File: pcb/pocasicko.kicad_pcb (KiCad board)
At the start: 2 copper layers, 100 x 100 mm, 15 parts, among them J1 SMA, J2 Header_SMD_01x06, J3 FPC24, Q1 Si2312, SW1 SW_Push, SW2 SW_Push, SW3 SW_Push, SW4 SW_Push, SW5 SW_Push, U1 CMWX1ZZABZ-091, U2 BME680

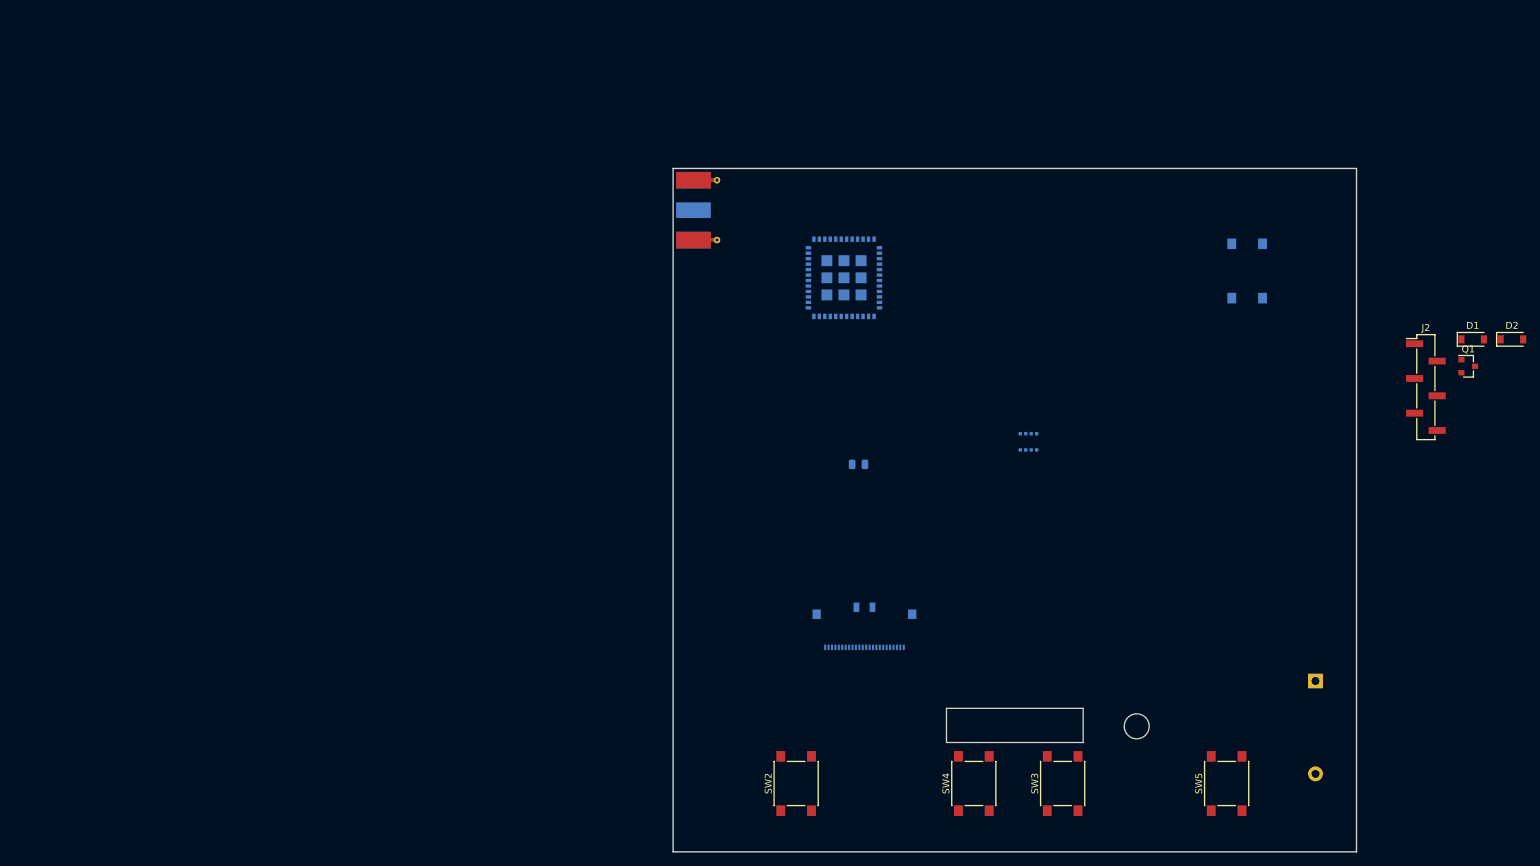
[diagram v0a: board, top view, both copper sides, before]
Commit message: Finish schematic and large component placement
All components chosen and placed on the PCB before routing and
schematic probably mostly finished.
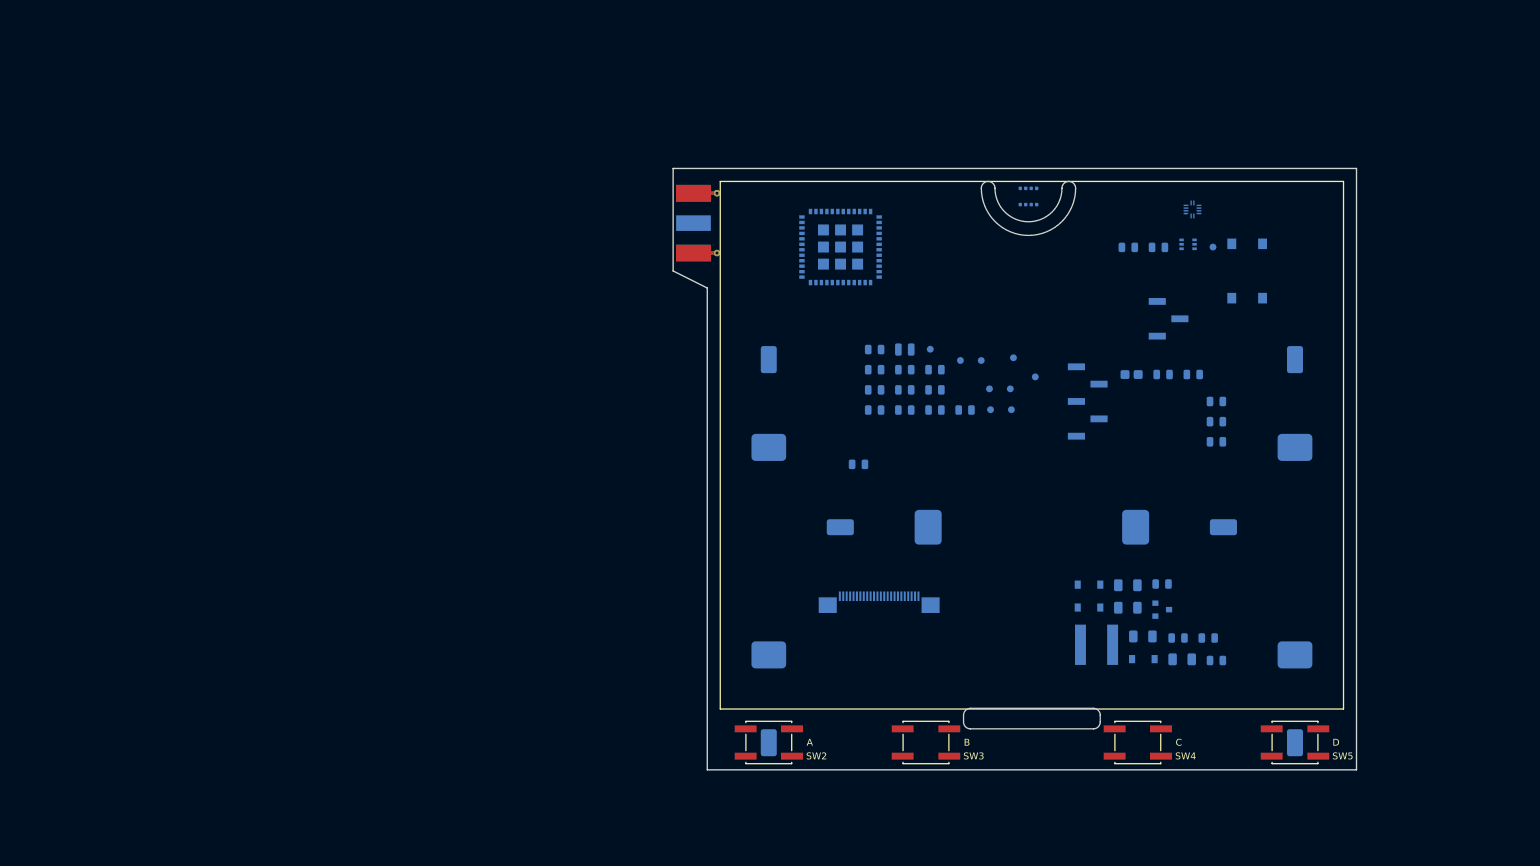
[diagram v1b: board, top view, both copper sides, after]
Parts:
- added BT2: AA, Moje:BatteryHolder_Keystone_53_1xAA, B.Cu at (152.5, 102.5)
- added BT3: AA, Moje:BatteryHolder_Keystone_53_1xAA, B.Cu at (114.0, 106.0)
- added C10: 1uF/6V, Capacitor_SMD:C_0805_2012Metric, B.Cu at (138.3, 85.3)
- added C11: 100nF, Capacitor_SMD:C_0805_2012Metric, B.Cu at (129.5, 76.5)
- added C12: 1uF/25V, Capacitor_SMD:C_0805_2012Metric, B.Cu at (133.9, 79.5)
- added C13: 1uF/25V, Capacitor_SMD:C_0805_2012Metric, B.Cu at (138.3, 82.4)
- added C14: 1uF/25V, Capacitor_SMD:C_0805_2012Metric, B.Cu at (142.7, 85.3)
- added C15: 1uF/50V, Capacitor_SMD:C_1206_3216Metric, B.Cu at (166.5, 114.3)
- added C16: 4.7uF/50V, Capacitor_SMD:C_1206_3216Metric, B.Cu at (168.7, 118.5)
- added C17: 10uF/6V, Capacitor_SMD:C_0805_2012Metric, B.Cu at (173.9, 118.7)
- added C18: 1uF/50V, Capacitor_SMD:C_1206_3216Metric, B.Cu at (174.5, 121.8)
- added C19: 100nF, Capacitor_SMD:C_0805_2012Metric, B.Cu at (179.5, 122.0)
- added C2: 10uF, Capacitor_SMD:C_0805_2012Metric, B.Cu at (129.5, 85.3)
- added C3: 10uF, Capacitor_SMD:C_0805_2012Metric, B.Cu at (179.5, 90.0)
- added C4: 1uF, Capacitor_SMD:C_0805_2012Metric, B.Cu at (171.7, 80.2)
- added C5: 100nF, Capacitor_SMD:C_0805_2012Metric, B.Cu at (179.5, 87.0)
- added C6: 10uF, Capacitor_SMD:C_0805_2012Metric, B.Cu at (129.5, 82.4)
- added C7: 1uF/25V, Capacitor_SMD:C_0805_2012Metric, B.Cu at (133.9, 85.3)
- added C8: 1uF/25V, Capacitor_SMD:C_0805_2012Metric, B.Cu at (129.5, 79.5)
- added C9: 1uF/25V, Capacitor_SMD:C_0805_2012Metric, B.Cu at (133.9, 82.4)
- added D3: LED, LED_SMD:LED_0805_2012Metric_Castellated, B.Cu at (167.1, 80.2)
- added D4: MBR0530, Diode_SMD:D_SOD-123, B.Cu at (160.9, 110.9)
- added G***: LOGO, Moje:moje_logo, B.Cu at (152.0, 70.5)
- added J4: Header_SMD_1x03, Connector_PinHeader_2.54mm:PinHeader_1x03_P2.54mm_Vertical_SMD_Pin1Left, B.Cu at (172.5, 72.0)
- added L1: DFE201612P-2R2M, Moje:L_0806_2016Metric, B.Cu at (133.9, 76.5)
- added L2: NRS6045T680MMGK, Inductor_SMD:L_Taiyo-Yuden_NR-60xx, B.Cu at (162.0, 119.7)
- added R1: 100k, Resistor_SMD:R_0805_2012Metric, B.Cu at (176.1, 80.2)
- added R2: 1k, Resistor_SMD:R_0805_2012Metric, B.Cu at (179.5, 84.1)
- added R3: 100k, Resistor_SMD:R_0805_2012Metric, B.Cu at (138.3, 79.5)
- added R4: 10k, Resistor_SMD:R_0805_2012Metric, B.Cu at (178.3, 118.7)
- added R5: 0R47, Resistor_SMD:R_1206_3216Metric, B.Cu at (166.5, 111.0)
- added R6: 0R, Resistor_SMD:R_0805_2012Metric, B.Cu at (171.6, 110.8)
- added R7: 0R, Resistor_SMD:R_0805_2012Metric, B.Cu at (166.6, 61.5)
- added R8: 0R, Resistor_SMD:R_0805_2012Metric, B.Cu at (171.0, 61.5)
- added TP1: CRF1, TestPoint:TestPoint_Pad_D1.0mm, B.Cu at (146.4, 85.3)
- added TP10: PB14, TestPoint:TestPoint_Pad_D1.0mm, B.Cu at (179.0, 61.5)
- added TP2: CRF2, TestPoint:TestPoint_Pad_D1.0mm, B.Cu at (137.6, 76.5)
- added TP3: CRF3, TestPoint:TestPoint_Pad_D1.0mm, B.Cu at (142.0, 78.1)
- added TP4: DIO0, TestPoint:TestPoint_Pad_D1.0mm, B.Cu at (146.3, 82.2)
- added TP5: DIO1, TestPoint:TestPoint_Pad_D1.0mm, B.Cu at (149.5, 85.3)
- added TP6: DIO2, TestPoint:TestPoint_Pad_D1.0mm, B.Cu at (149.8, 77.7)
- added TP7: DIO3, TestPoint:TestPoint_Pad_D1.0mm, B.Cu at (145.1, 78.1)
- added TP8: DIO4, TestPoint:TestPoint_Pad_D1.0mm, B.Cu at (149.3, 82.2)
- added TP9: DIO5, TestPoint:TestPoint_Pad_D1.0mm, B.Cu at (153.0, 80.5)
- added U3: MP28200, Moje:QFN-12_2x2_Pitch0.4mm, B.Cu at (176.0, 56.0)
- added U4: LM66100, Package_TO_SOT_SMD:SOT-363_SC-70-6, B.Cu at (175.3, 61.1)
- BT1: value 2xAA -> AA; footprint Battery:BatteryHolder_MPD_BC2AAPC_2xAA -> Moje:BatteryHolder_Keystone_53_1xAA
- D1, D2: value D_Schottky -> MBR0530; moved to B.Cu
- J2: value Header_SMD_01x06 -> Header_SMD_1x05; footprint Connector_PinHeader_2.54mm:PinHeader_1x06_P2.54mm_Vertical_SMD_Pin1Left -> Connector_PinHeader_2.54mm:PinHeader_1x05_P2.54mm_Vertical_SMD_Pin1Left; moved to B.Cu
- J3: footprint Connector_FFC-FPC:Molex_502244-2430_1x24-1MP_P0.5mm_Horizontal -> Moje:Waveshare_EPD_4.2_Amphenol_SFV24R-4STBE1HLF
- Q1: value Si2312 -> AO3400A; moved to B.Cu
- SW2: value SW_Push -> A; footprint Button_Switch_SMD:SW_Push_1P1T_NO_6x6mm_H9.5mm -> Button_Switch_SMD:SW_SPST_EVQQ2
- SW3: value SW_Push -> B; footprint Button_Switch_SMD:SW_Push_1P1T_NO_6x6mm_H9.5mm -> Button_Switch_SMD:SW_SPST_EVQQ2
- SW4: value SW_Push -> C; footprint Button_Switch_SMD:SW_Push_1P1T_NO_6x6mm_H9.5mm -> Button_Switch_SMD:SW_SPST_EVQQ2
- SW5: value SW_Push -> D; footprint Button_Switch_SMD:SW_Push_1P1T_NO_6x6mm_H9.5mm -> Button_Switch_SMD:SW_SPST_EVQQ2
- moved D2 71.4 mm to (168.8, 121.8)
- moved D1 68.5 mm to (160.9, 114.2)
- moved Q1 57.2 mm to (171.6, 114.6)
- moved J2 49.5 mm to (160.7, 84.1)
- moved J3 36.8 mm to (152.5, 89.5), turned to 180 degrees
- moved U2 35.9 mm to (152.0, 54.1)
- moved SW4 24.7 mm to (168.0, 134.0), turned to 0 degrees
- moved SW3 20.9 mm to (137.0, 134.0), turned to 0 degrees
- moved BT1 19.2 mm to (191.0, 106.0), turned to -90 degrees
- moved SW5 11.7 mm to (191.0, 134.0), turned to 0 degrees
- moved SW2 7.21 mm to (114.0, 134.0), turned to 0 degrees
- moved U1 4.53 mm to (124.5, 61.5), turned to 180 degrees
- moved J1 1.90 mm to (104.7, 58.0)
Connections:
- net Net-(J3-Pad19) renamed /VPP
- net Net-(J3-Pad6) renamed /TSCL
- net Net-(J3-Pad7) renamed /TSDA
- net Net-(U1-Pad35) renamed /BME680_SCL
- net Net-(U1-Pad36) renamed /BME680_SDA
- BT1 pad 1: +BATT -> Net-(BT1-Pad1)
- BT1 pad 2: Net-(BT1-Pad2) -> GND
- C1 pad 1: /Reset -> /~MCU_RESET
- C1 pad 2: Net-(C1-Pad2) -> GND
- D1 pad 1: Net-(C2-Pad1) -> GND
- D1 pad 2: Net-(D1-Pad2) -> Net-(C16-Pad2)
- D2 pad 1: Net-(D2-Pad1) -> Net-(C16-Pad2)
- D2 pad 2: Net-(C2-Pad1) -> /PREVGL
- J2 pad 1: Net-(J2-Pad1) -> +2V5
- J2 pad 5: /NRST -> /~MCU_RESET
- J3 pad 10: Net-(J3-Pad10) -> /RES#
- J3 pad 11: Net-(J3-Pad11) -> /D/C#
- J3 pad 12: Net-(J3-Pad12) -> /CS#
- J3 pad 13: Net-(J3-Pad13) -> /SCLK
- J3 pad 14: Net-(J3-Pad14) -> /SDI
- J3 pad 15: Net-(J3-Pad15) -> +2V5
- J3 pad 16: Net-(J3-Pad16) -> +2V5
- J3 pad 17: Net-(J3-Pad17) -> GND
- J3 pad 18: Net-(J3-Pad18) -> /VDD
- J3 pad 2: Net-(J3-Pad2) -> /GDR
- J3 pad 20: Net-(J3-Pad20) -> /VSH
- J3 pad 21: Net-(J3-Pad21) -> /PREVGH
- J3 pad 22: Net-(J3-Pad22) -> /VSL
- J3 pad 23: Net-(J3-Pad23) -> /PREVGL
- J3 pad 24: Net-(J3-Pad24) -> /VCOM
- J3 pad 3: Net-(J3-Pad3) -> /RESE
- J3 pad 4: Net-(J3-Pad4) -> /VGL
- J3 pad 5: Net-(J3-Pad5) -> /VGH
- J3 pad 8: Net-(J3-Pad8) -> /BS1
- J3 pad 9: Net-(J3-Pad9) -> /BUSY
- Q1 pad 1: +BATT -> /GDR
- Q1 pad 2: GND -> /RESE
- Q1 pad 3: Net-(BT1-Pad2) -> Net-(C16-Pad1)
- SW1 pad 2: Net-(C1-Pad2) -> /~MCU_RESET
- SW2 pad 1: Net-(SW2-Pad1) -> /BUTTON_A
- SW2 pad 2: Net-(SW2-Pad2) -> GND
- SW3 pad 1: Net-(SW3-Pad1) -> /BUTTON_B
- SW3 pad 2: Net-(SW3-Pad2) -> GND
- SW4 pad 1: Net-(SW4-Pad1) -> /BUTTON_C
- SW4 pad 2: Net-(SW4-Pad2) -> GND
- SW5 pad 1: Net-(SW5-Pad1) -> /BUTTON_D
- SW5 pad 2: Net-(SW5-Pad2) -> GND
- U1 pad 14: Net-(U1-Pad14) -> /SDI
- U1 pad 16: Net-(U1-Pad16) -> /SCLK
- U1 pad 17: Net-(U1-Pad17) -> /CS#
- U1 pad 18: Net-(U1-Pad18) -> /USART1_RX
- U1 pad 19: Net-(U1-Pad19) -> /USART1_TX
- U1 pad 2: Net-(U1-Pad2) -> /LED
- U1 pad 21: Net-(U1-Pad21) -> /BUTTON_D
- U1 pad 22: Net-(U1-Pad22) -> /BUTTON_C
- U1 pad 23: Net-(U1-Pad23) -> /BUTTON_B
- U1 pad 24: Net-(U1-Pad24) -> /BATT_VOLTAGE
- U1 pad 32: Net-(U1-Pad32) -> +2V5
- U1 pad 33: Net-(U1-Pad33) -> /BUTTON_A
- U1 pad 34: /Reset -> /~MCU_RESET
- U1 pad 37: Net-(U1-Pad37) -> /D/C#
- U1 pad 39: Net-(U1-Pad39) -> /RES#
- U1 pad 4: Net-(U1-Pad4) -> +2V5
- U1 pad 40: Net-(U1-Pad40) -> /BUSY
- U1 pad 41: /SWCLK -> /SWDIO
- U1 pad 42: /SWDIO -> /SWCLK
- U1 pad 46: Net-(U1-Pad46) -> /TCXO_OUT
- U1 pad 47: Net-(U1-Pad47) -> /TCXO_OUT
- U1 pad 48: Net-(U1-Pad48) -> Net-(U1-Pad1)
- U1 pad 5: Net-(U1-Pad5) -> +2V5
- U1 pad 6: Net-(U1-Pad6) -> +2V5
- U2 pad 6: +3V3 -> +2V5
- U2 pad 8: +3V3 -> +2V5
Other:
- board size 100 x 100 mm -> 100 x 88 mm
- board text added: "Počasíčko 10/2019 Rev.1 Radovan Blažek"

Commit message: Routing progress
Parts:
- added C20: 1uF, Capacitor_SMD:C_0805_2012Metric, B.Cu at (116.0, 59.1)
- added H1: M3_Hole, MountingHole:MountingHole_3.2mm_M3_DIN965_Pad, F.Cu at (126.0, 134.0)
- added H2: M3_Hole, MountingHole:MountingHole_3.2mm_M3_DIN965_Pad, F.Cu at (180.0, 134.0)
- added REF**: KiCad-Logo_5mm_SilkScreen, Symbol:KiCad-Logo_5mm_SilkScreen, B.Cu at (187.9, 58.6)
- moved R7 56.9 mm to (110.6, 71.5)
- moved R1 56.1 mm to (126.8, 53.5)
- moved C3 55.5 mm to (133.9, 58.4), turned to 180 degrees
- moved C19 54.2 mm to (127.0, 108.5), turned to -90 degrees
- moved R2 53.3 mm to (133.9, 56.5)
- moved C5 52.9 mm to (133.9, 60.3), turned to 180 degrees
- moved TP10 52.3 mm to (127.3, 69.6)
- moved TP6 51.1 mm to (138.7, 27.9)
- moved TP8 51.1 mm to (138.2, 32.4)
- moved TP9 51.1 mm to (141.9, 30.6)
- moved TP4 51.1 mm to (135.2, 32.4)
- moved TP5 51.1 mm to (138.4, 35.5)
- moved TP7 51.1 mm to (134.0, 28.2)
- moved R6 50.6 mm to (121.0, 108.5), turned to 90 degrees
- moved U3 48.6 mm to (141.7, 90.4), turned to 180 degrees
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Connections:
- C12 pad 2: +2V5 -> /VPP
- U2 pad 2: +3V3 -> +2V5
- U3 pad 1: Net-(L1-Pad1) -> +2V5
- U3 pad 9: +2V5 -> Net-(L1-Pad1)
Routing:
- net /D/C#: track 0.00 -> 106.9 mm, vias 0 -> 2
- net /RES#: track 0.00 -> 101.8 mm, vias 0 -> 2
- net /BUSY: track 0.00 -> 97.2 mm, vias 0 -> 2
- net /SDI: track 0.00 -> 76.4 mm, vias 0 -> 2
- net /SCLK: track 0.00 -> 73.0 mm, vias 0 -> 2
- net /CS#: track 0.00 -> 70.1 mm, vias 0 -> 2
- net +2V5: track 0.00 -> 60.5 mm, vias 0 -> 2
- net /~MCU_RESET: track 0.00 -> 59.0 mm, vias 0 -> 2
- net Net-(BT2-Pad1): track 0.00 -> 53.1 mm
- net GND: track 0.00 -> 51.7 mm, vias 0 -> 42
- net /BME680_SCL: track 0.00 -> 47.6 mm
- net Net-(BT1-Pad1): track 0.00 -> 45.4 mm
- net /BME680_SDA: track 0.00 -> 43.6 mm
- net /GDR: track 0.00 -> 36.7 mm
- net /RESE: track 0.00 -> 30.6 mm
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- added copper zone on B.Cu, net +2V5
- added copper zone on B.Cu, net /BATT_VOLTAGE
- added copper zone on B.Cu, net GND
- added copper zone on F.Cu, net GND
- added copper zone on B.Cu, net Net-(J1-Pad1)
- added copper zone on B.Cu, net Net-(L1-Pad1)
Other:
- net class Default: clearance 0.2 -> 0.127
- rule pad_to_mask_clearance: 0.051 -> 0
- rule solder_mask_min_width: 0.25 -> 0.12
- rule trace_clearance: 0.2 -> 0.127
- rule trace_min: 0.2 -> 0.127
- rule via_min_size: 0.4 -> 0.6
- board text added: "GND"
- board text added: "NRST"
- board text added: "RX"
- board text added: "SWCLK"
- board text added: "SWDIO"
- board text added: "TX"
- board text added: "VDD"

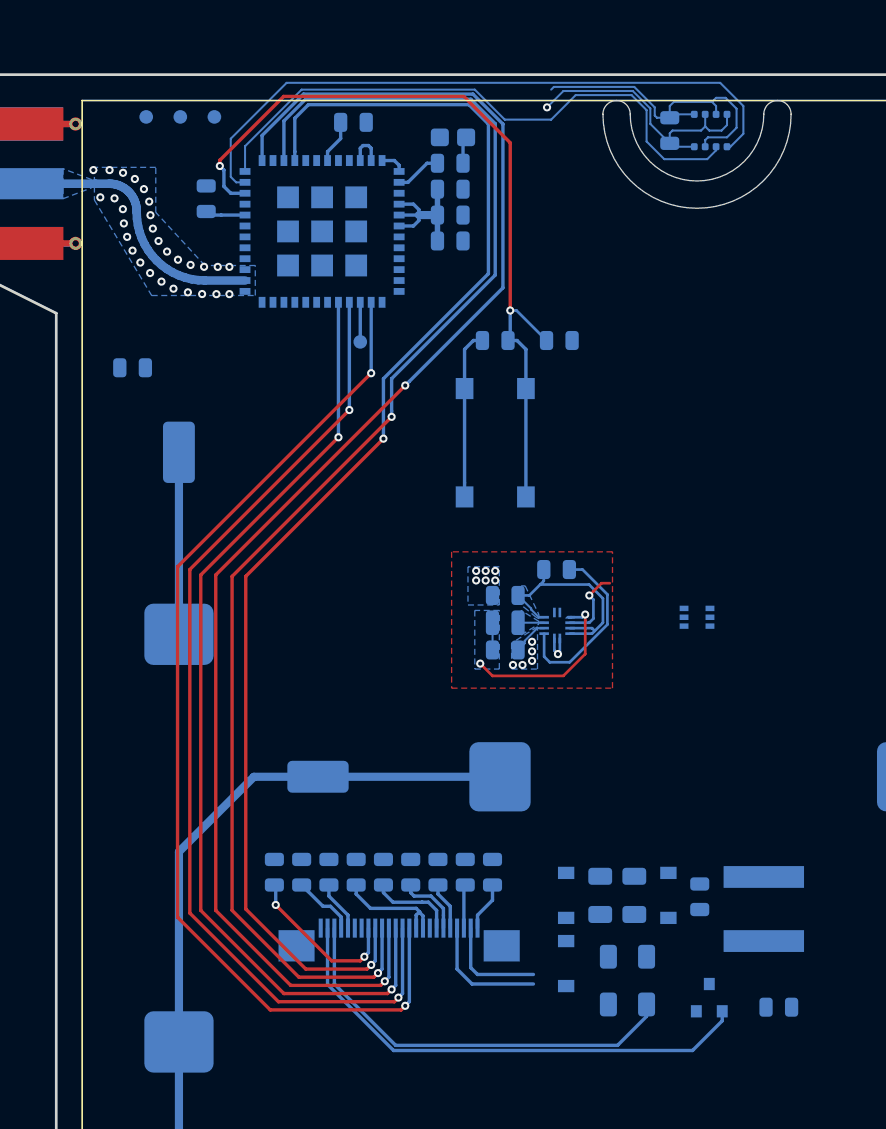
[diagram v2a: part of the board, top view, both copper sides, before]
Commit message: Rotate LoRa module
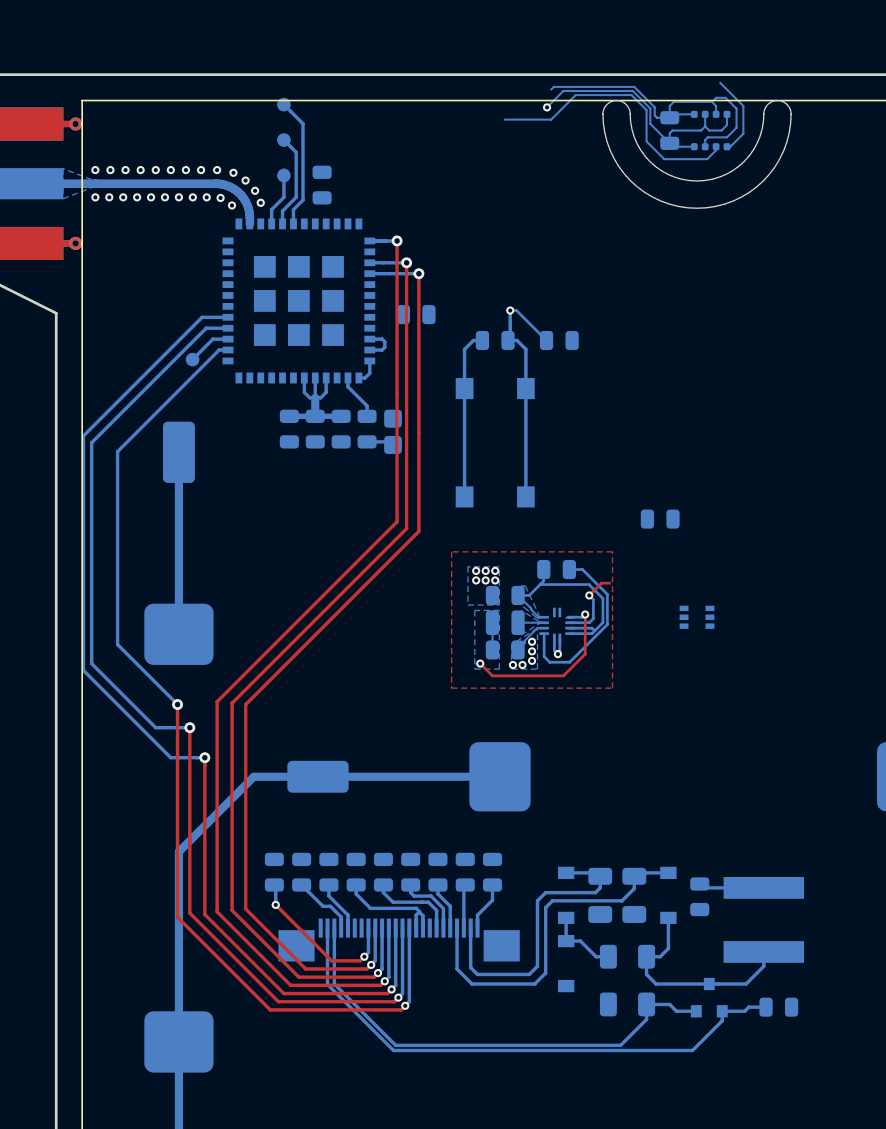
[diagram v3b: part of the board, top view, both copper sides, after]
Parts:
- moved R7 40.3 mm to (149.3, 82.6)
- moved D3 22.0 mm to (129.7, 76.2), turned to -90 degrees
- moved R2 20.4 mm to (127.8, 76.0), turned to -90 degrees
- moved C3 19.3 mm to (125.9, 76.0), turned to 90 degrees
- moved C5 18.6 mm to (124.0, 76.0), turned to 90 degrees
- moved C4 18.2 mm to (122.1, 76.0), turned to 90 degrees
- moved R1 14.8 mm to (131.4, 67.6)
- moved TP10 12.4 mm to (115.0, 70.9)
- moved TP3 10.2 mm to (121.7, 54.8), turned to -90 degrees
- moved C20 8.56 mm to (124.5, 58.1)
- moved TP2 7.65 mm to (121.7, 52.2), turned to -90 degrees
- moved TP1 6.67 mm to (121.7, 57.4), turned to -90 degrees
- moved U1 5.38 mm to (122.8, 66.6), turned to 90 degrees
- moved L2 0.80 mm to (156.9, 112.0)
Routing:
- net /BME680_SCL: track 47.6 -> 6.04 mm
- net /~MCU_RESET: track 59.0 -> 18.2 mm, vias 2 -> 1
- net /D/C#: track 106.9 -> 76.6 mm
- net /RES#: track 101.8 -> 71.8 mm
- net /BUSY: track 97.2 -> 69.4 mm
- net /BME680_SDA: track 43.6 -> 20.1 mm
- net /PREVGH: track 9.06 -> 25.7 mm
- net Net-(C16-Pad1): track 0.00 -> 15.9 mm
- net /PREVGL: track 7.71 -> 21.5 mm
- net Net-(TP2-Pad1): track 0.00 -> 9.62 mm
- net Net-(TP3-Pad1): track 0.00 -> 6.94 mm
- net Net-(C16-Pad2): track 0.00 -> 5.28 mm
- net /CS#: track 70.1 -> 75.3 mm
- net Net-(TP1-Pad1): track 0.00 -> 4.32 mm
- net /RESE: track 30.6 -> 34.6 mm
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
